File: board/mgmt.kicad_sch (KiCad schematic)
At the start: 80 parts, among them J3 JUMPER_0402_SPDT, J4 JUMPER_0402_SPDT, J5 RJ45, J9 XILINX_JTAG, SW1 SWITCH, SW2 SWITCH, SW3 SWITCH, SW4 SWITCH, SW5 SWITCH, SW7 BUTTON, U13 STM32H735-UFBGA176-25, U3 MAX232

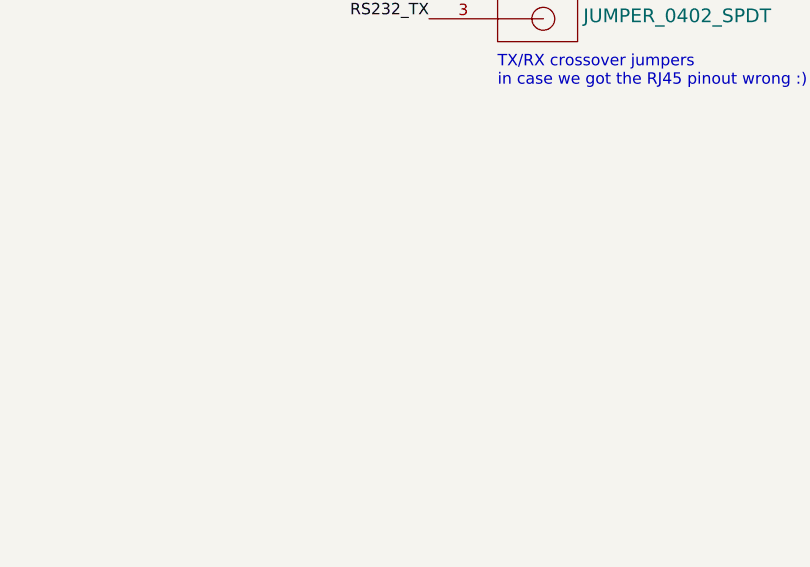
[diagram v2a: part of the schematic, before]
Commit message: Finished schematic review. Added a few more test points.
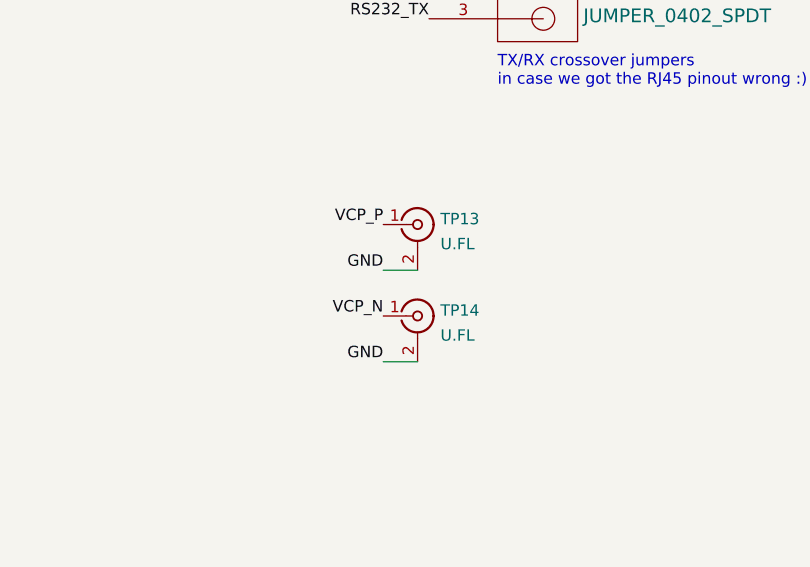
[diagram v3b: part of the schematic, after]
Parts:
- added TP13, TP14: U.FL, azonenberg_pcb:CONN_U.FL_TE_1909763-1, symbol conn:CONN_COAXIAL
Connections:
- net GND: now also TP13.2 (Ext), TP14.2 (Ext)
- net VCP_N: now also TP14.1 (In)
- net VCP_P: now also TP13.1 (In)
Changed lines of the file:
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@@
+    (stroke (width 0) (type default) (color 0 0 0 0))
+  )
+  (wire (pts (xy 341.63 124.46) (xy 345.44 124.46))
     (stroke (width 0) (type default) (color 0 0 0 0))
   )
@@
   )
   (wire (pts (xy 105.41 148.59) (xy 128.27 148.59))
+    (stroke (width 0) (type default) (color 0 0 0 0))
+  )
+  (wire (pts (xy 341.63 114.3) (xy 345.44 114.3))
     (stroke (width 0) (type default) (color 0 0 0 0))
   )
@@
     (effects (font (size 1.27 1.27)) (justify left bottom))
   )
+  (label "VCP_P" (at 341.63 109.22 180)
+    (effects (font (size 1.27 1.27)) (justify right bottom))
+  )
   (label "RS232_TX_RJ45" (at 350.52 41.91 180)
     (effects (font (size 1.27 1.27)) (justify right bottom))
@@
     (effects (font (size 1.27 1.27)) (justify right bottom))
   )
+  (label "VCP_N" (at 341.63 119.38 180)
+    (effects (font (size 1.27 1.27)) (justify right bottom))
+  )
   (label "3V3" (at 38.1 109.22 180)
     (effects (font (size 1.27 1.27)) (justify right bottom))
@@
     (effects (font (size 1.27 1.27)) (justify right bottom))
   )
+  (label "GND" (at 341.63 124.46 180)
+    (effects (font (size 1.27 1.27)) (justify right bottom))
+  )
   (label "VDDA" (at 58.42 200.66 0)
     (effects (font (size 1.27 1.27)) (justify left bottom))
@@
   (label "GND" (at 370.84 59.69 0)
     (effects (font (size 1.27 1.27)) (justify left bottom))
+  )
+  (label "GND" (at 341.63 114.3 180)
+    (effects (font (size 1.27 1.27)) (justify right bottom))
   )
   (label "C1_N" (at 271.78 45.72 180)
@@
     )
     (property "Datasheet" "" (id 3) (at 113.03 184.15 0)
+      (effects (font (size 1.27 1.27)) hide)
+    )
+    (pin "1")
+    (pin "2")
+  )
+  (symbol (lib_id "conn:CONN_COAXIAL") (at 345.44 109.22 0) (unit 1)
+    (in_bom yes) (on_board yes) (fields_autoplaced)
+    (property "Reference" "TP13" (id 0) (at 347.9801 108.6047 0)
+      (effects (font (size 1.27 1.27)) (justify left))
+    )
+    (property "Value" "U.FL" (id 1) (at 347.9801 111.3798 0)
+      (effects (font (size 1.27 1.27)) (justify left))
+    )
+    (property "Footprint" "azonenberg_pcb:CONN_U.FL_TE_1909763-1" (id 2) (at 345.44 109.22 0)
+      (effects (font (size 1.27 1.27)) hide)
+    )
+    (property "Datasheet" "" (id 3) (at 345.44 109.22 0)
       (effects (font (size 1.27 1.27)) hide)
     )
@@
     (pin "9")
   )
+  (symbol (lib_id "conn:CONN_COAXIAL") (at 345.44 119.38 0) (unit 1)
+    (in_bom yes) (on_board yes) (fields_autoplaced)
+    (property "Reference" "TP14" (id 0) (at 347.9801 118.7647 0)
+      (effects (font (size 1.27 1.27)) (justify left))
+    )
+    (property "Value" "U.FL" (id 1) (at 347.9801 121.5398 0)
+      (effects (font (size 1.27 1.27)) (justify left))
+    )
+    (property "Footprint" "azonenberg_pcb:CONN_U.FL_TE_1909763-1" (id 2) (at 345.44 119.38 0)
+      (effects (font (size 1.27 1.27)) hide)
+    )
+    (property "Datasheet" "" (id 3) (at 345.44 119.38 0)
+      (effects (font (size 1.27 1.27)) hide)
+    )
+    (pin "1")
+    (pin "2")
+  )
   (symbol (lib_id "device:C") (at 85.09 184.15 0) (unit 1)

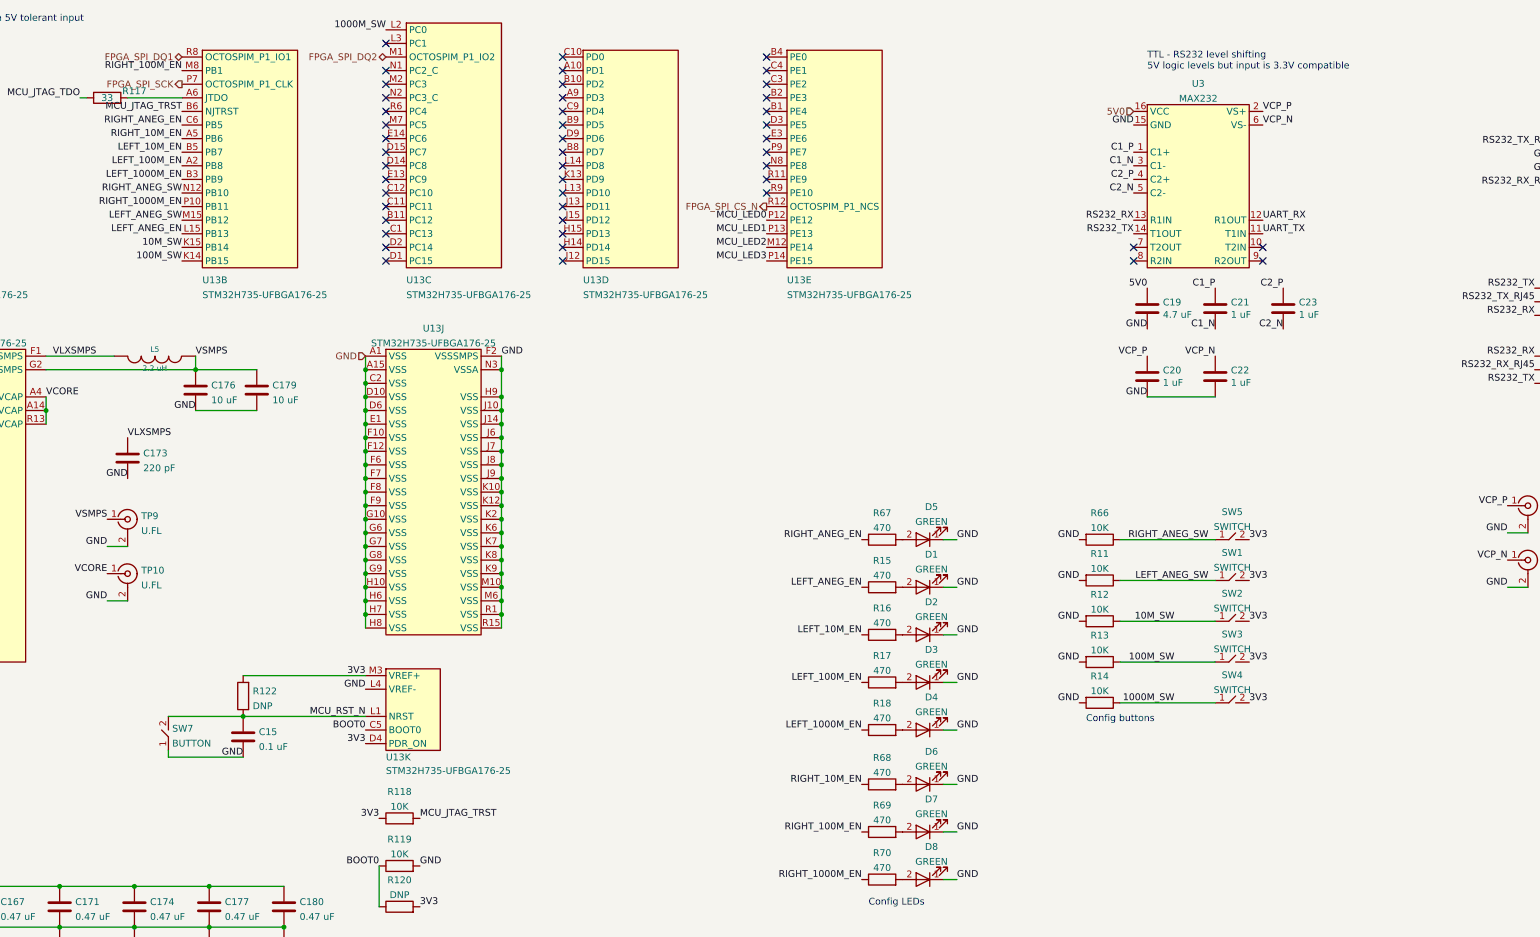
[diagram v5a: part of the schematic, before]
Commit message: Good progress on initial layout of MCU subsystem
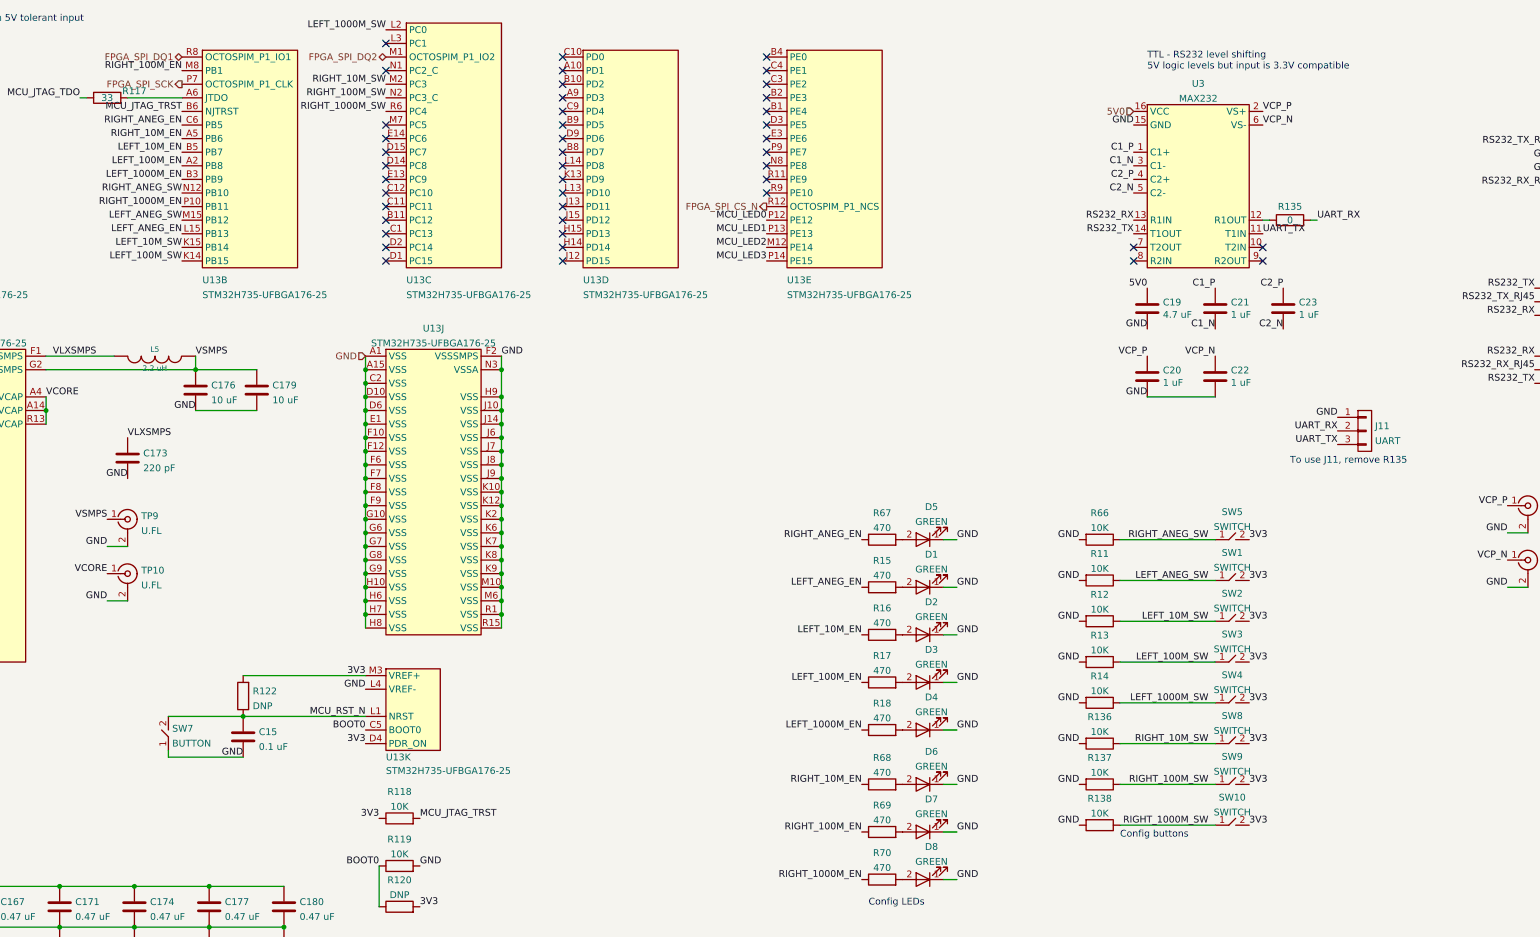
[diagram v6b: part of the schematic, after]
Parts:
- added J11: UART, azonenberg_pcb:CONN_HEADER_2.54MM_1x3, symbol conn:CONN_01X03
- added R135: 0, azonenberg_pcb:EIA_0402_RES_NOSILK, symbol device:R
- added R136, R137, R138: 10K, azonenberg_pcb:EIA_0402_RES_NOSILK, symbol device:R
- added SW10, SW8, SW9: SWITCH, azonenberg_pcb:SWITCH_RAFI_MICON_5, symbol passive-azonenberg:SWITCH
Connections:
- net 3V3: now also SW10.2, SW8.2, SW9.2
- net GND: now also J11.1 (P1), R136.2, R137.2, R138.2
- net UART_RX: now also J11.2 (P2), R135.2; no longer U3.12 (R1OUT)
- net UART_TX: now also J11.3 (P3)
- net RIGHT_10M_SW: now reaches U13.M2 (PC3)
- net RIGHT_10M_SW: now also R136.1, SW8.1
- net RIGHT_100M_SW: now reaches U13.N2 (PC3_C)
- net RIGHT_100M_SW: now also R137.1, SW9.1
- net RIGHT_1000M_SW: now reaches U13.R6 (PC4)
- net RIGHT_1000M_SW: now also R138.1, SW10.1
- net 1000M_SW renamed LEFT_1000M_SW
- net 100M_SW renamed LEFT_100M_SW
- net 10M_SW renamed LEFT_10M_SW
- new net: R135.1, U3.12 (R1OUT)
- no-connect marks 63 -> 60
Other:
- note added: "To use J11, remove R135"

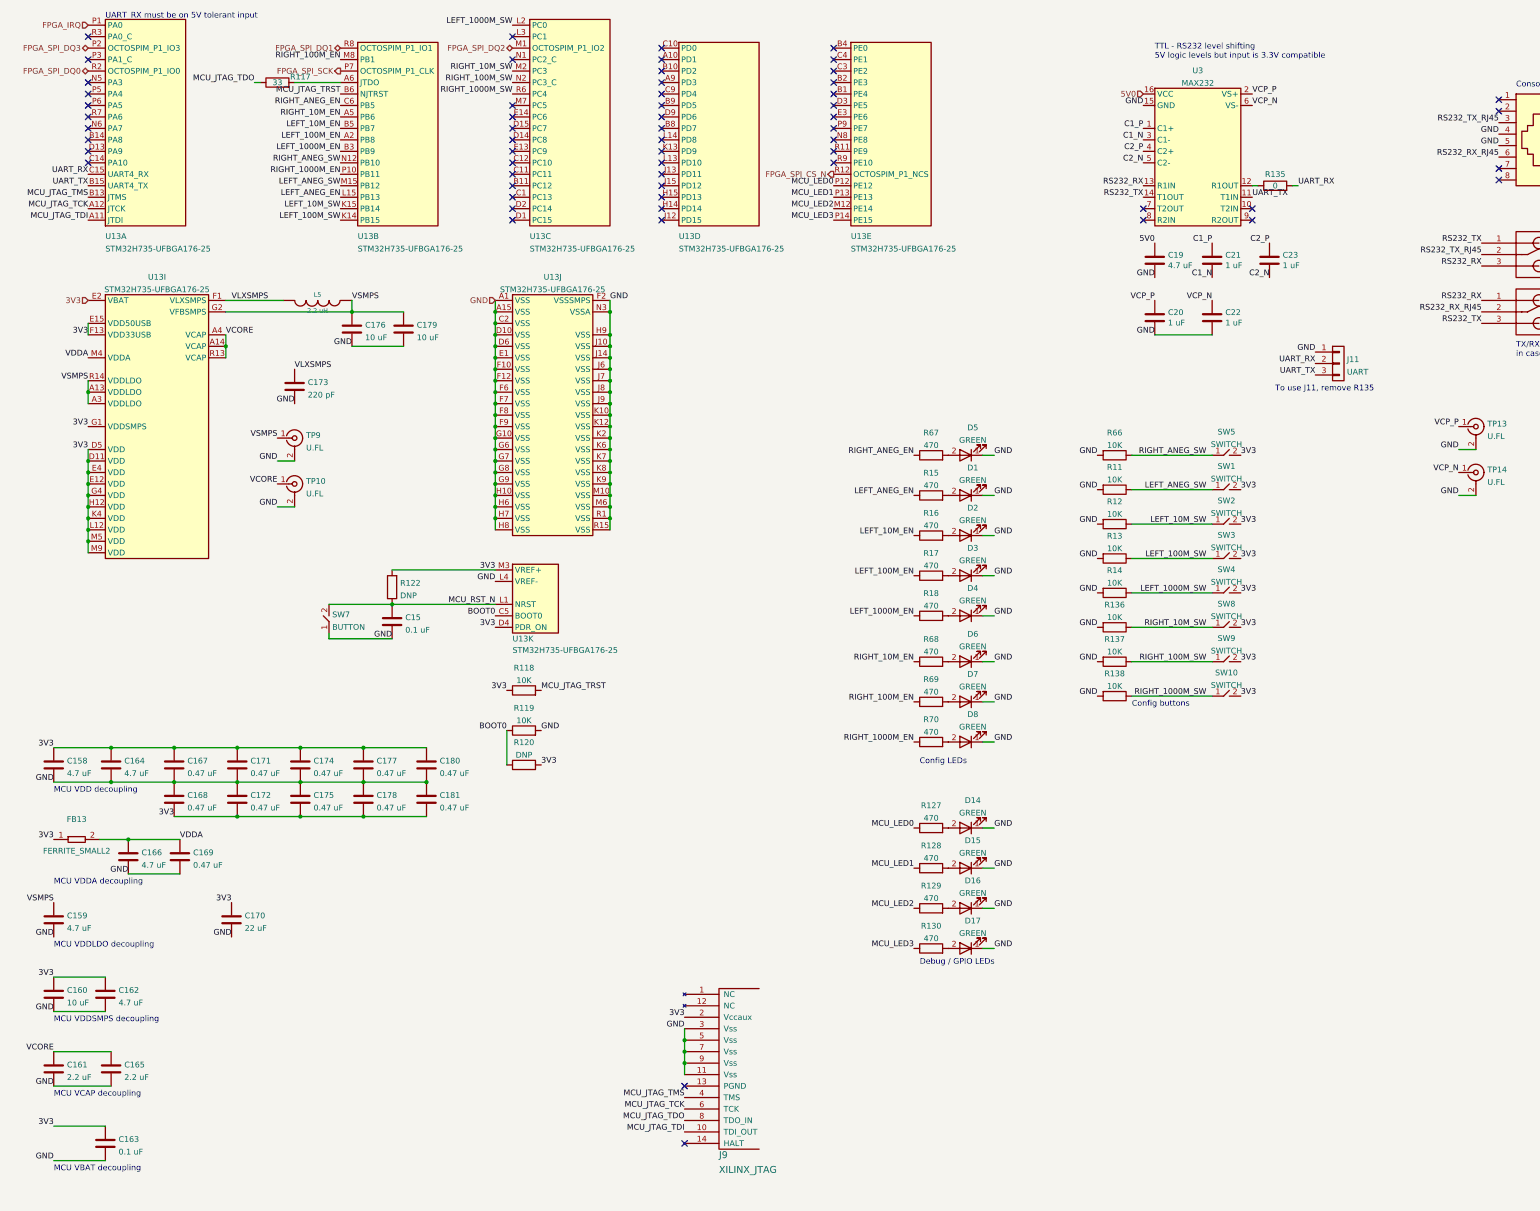
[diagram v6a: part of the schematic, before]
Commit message: Updating file: ethernet-tap.kicad_pcb with current fully routed design.
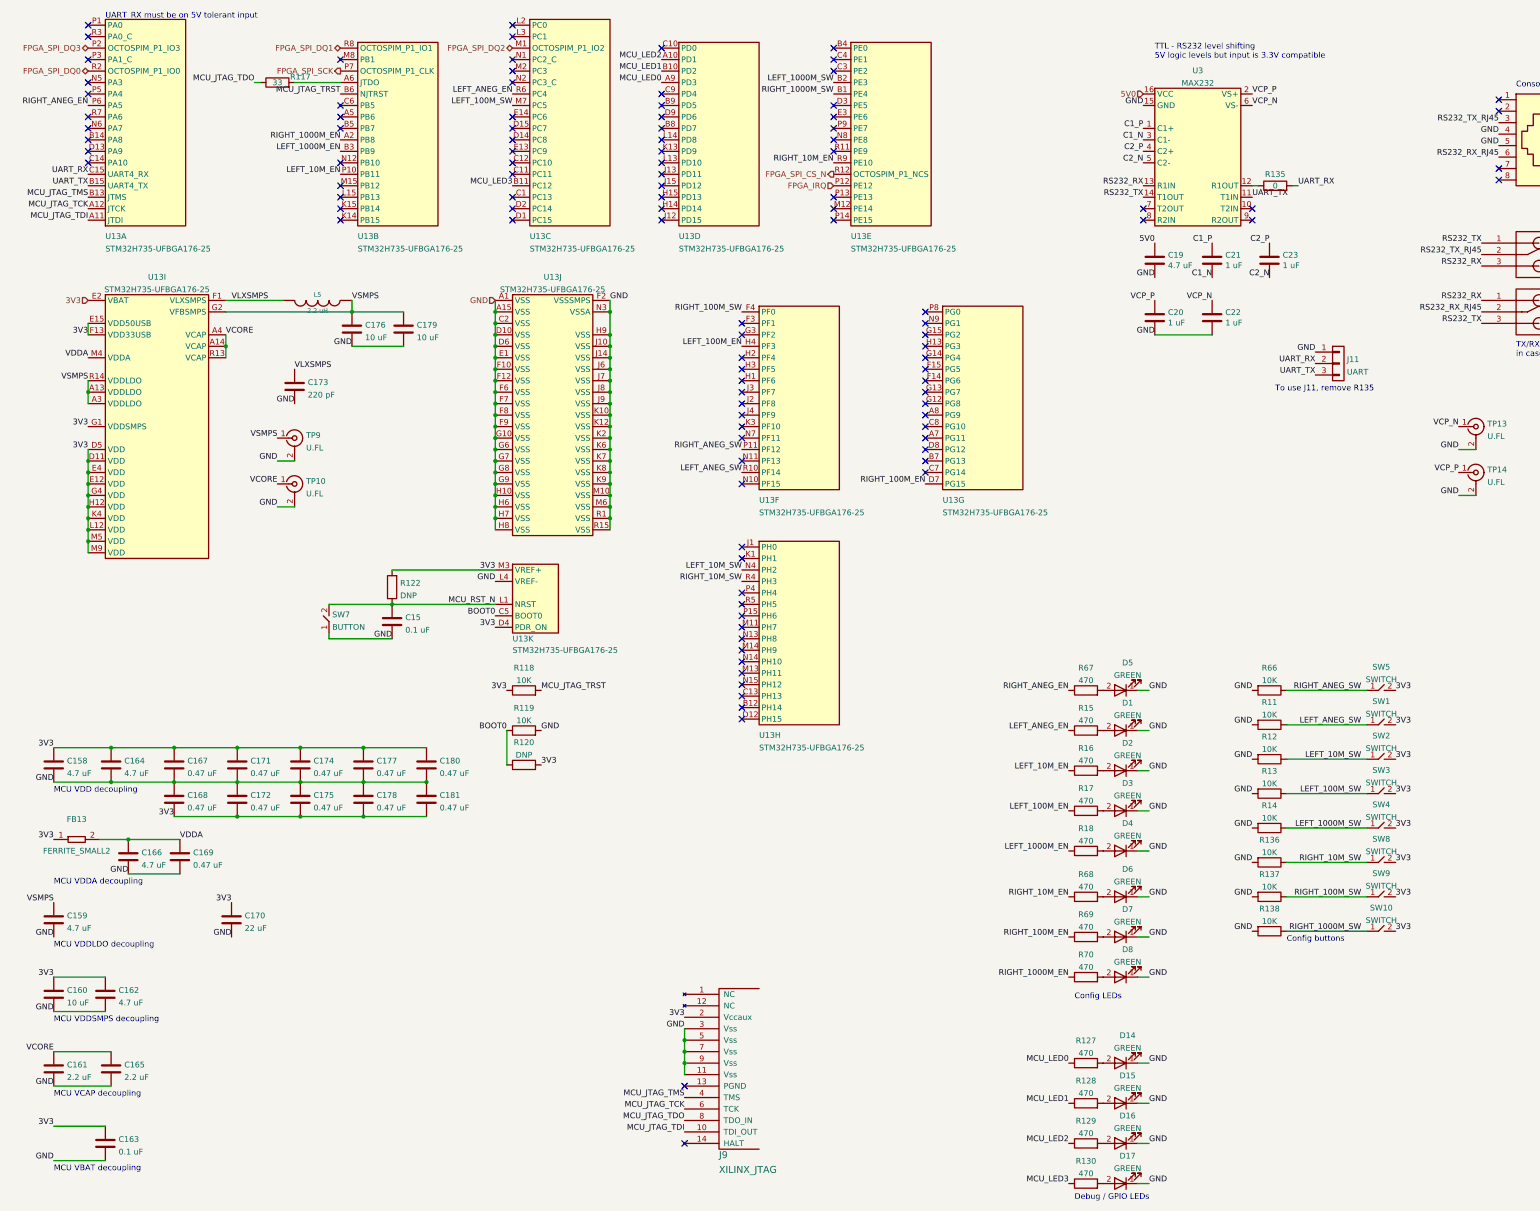
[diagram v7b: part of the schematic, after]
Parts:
- added unit 6 of U13
- added unit 7 of U13
- added unit 8 of U13
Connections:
- net FPGA_IRQ: now also U13.P12 (PE12); no longer U13.P1 (PA0)
- net LEFT_1000M_SW: now also U13.B2 (PE3); no longer U13.L2 (PC0)
- net LEFT_100M_EN: now also U13.H4 (PF3); no longer U13.A2 (PB8)
- net LEFT_100M_SW: now also U13.M7 (PC5); no longer U13.K14 (PB15)
- net LEFT_10M_EN: now also U13.P10 (PB11); no longer U13.B5 (PB7)
- net LEFT_10M_SW: now also U13.N4 (PH2); no longer U13.K15 (PB14)
- net LEFT_ANEG_EN: now also U13.R6 (PC4); no longer U13.L15 (PB13)
- net LEFT_ANEG_SW: now also U13.R10 (PF14); no longer U13.M15 (PB12)
- net MCU_LED0: now also U13.A9 (PD3); no longer U13.P12 (PE12)
- net MCU_LED1: now also U13.B10 (PD2); no longer U13.P13 (PE13)
- net MCU_LED2: now also U13.A10 (PD1); no longer U13.M12 (PE14)
- net MCU_LED3: now also U13.B11 (PC12); no longer U13.P14 (PE15)
- net RIGHT_1000M_EN: now also U13.A2 (PB8); no longer U13.P10 (PB11)
- net RIGHT_1000M_SW: now also U13.B1 (PE4); no longer U13.R6 (PC4)
- net RIGHT_100M_EN: now also U13.D7 (PG15); no longer U13.M8 (PB1)
- net RIGHT_100M_SW: now also U13.F4 (PF0); no longer U13.N2 (PC3_C)
- net RIGHT_10M_EN: now also U13.R9 (PE10); no longer U13.A5 (PB6)
- net RIGHT_10M_SW: now also U13.R4 (PH3); no longer U13.M2 (PC3)
- net RIGHT_ANEG_EN: now also U13.P6 (PA5); no longer U13.C6 (PB5)
- net RIGHT_ANEG_SW: now also U13.P11 (PF12); no longer U13.N12 (PB10)
- net VCP_N: now also TP13.1 (In); no longer TP14.1 (In)
- net VCP_P: now also TP14.1 (In); no longer TP13.1 (In)
- no-connect marks 60 -> 108
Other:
- moved on the sheet: D1, D14, D15, D16, D17, D2, D3, D4, D5, D6, D7, D8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
